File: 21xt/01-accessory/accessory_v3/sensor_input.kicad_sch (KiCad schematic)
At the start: 3 parts, among them J1 Conn_02x23_Counter_Clockwise, J2 Mezzanine Edge

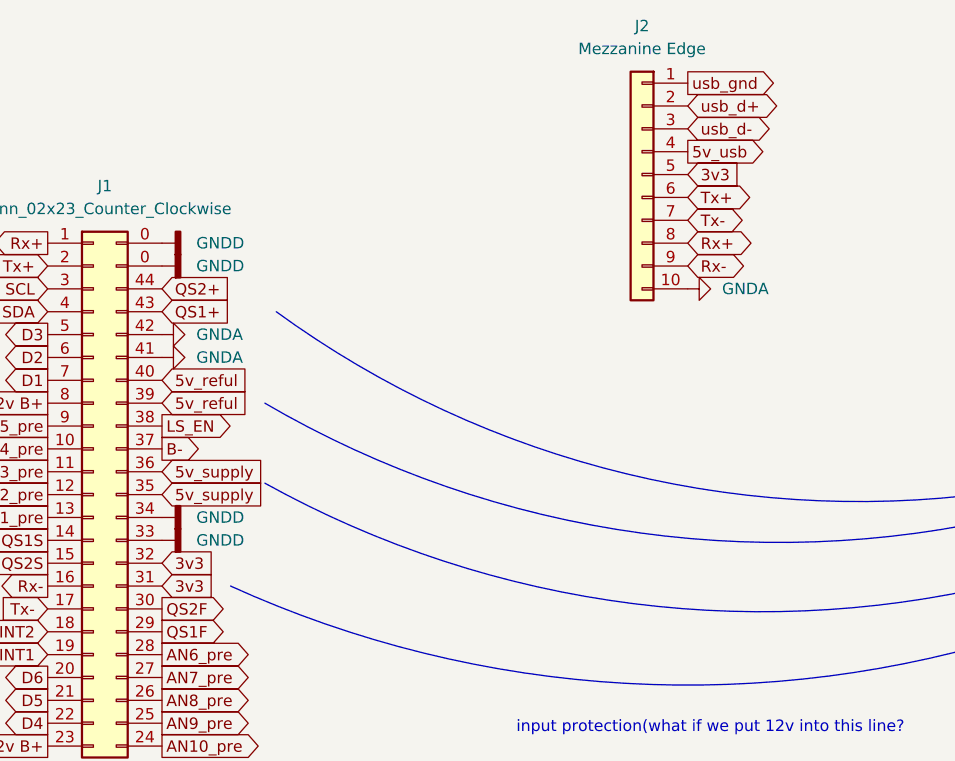
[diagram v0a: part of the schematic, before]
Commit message: Rerouted and connected 3v3 nets
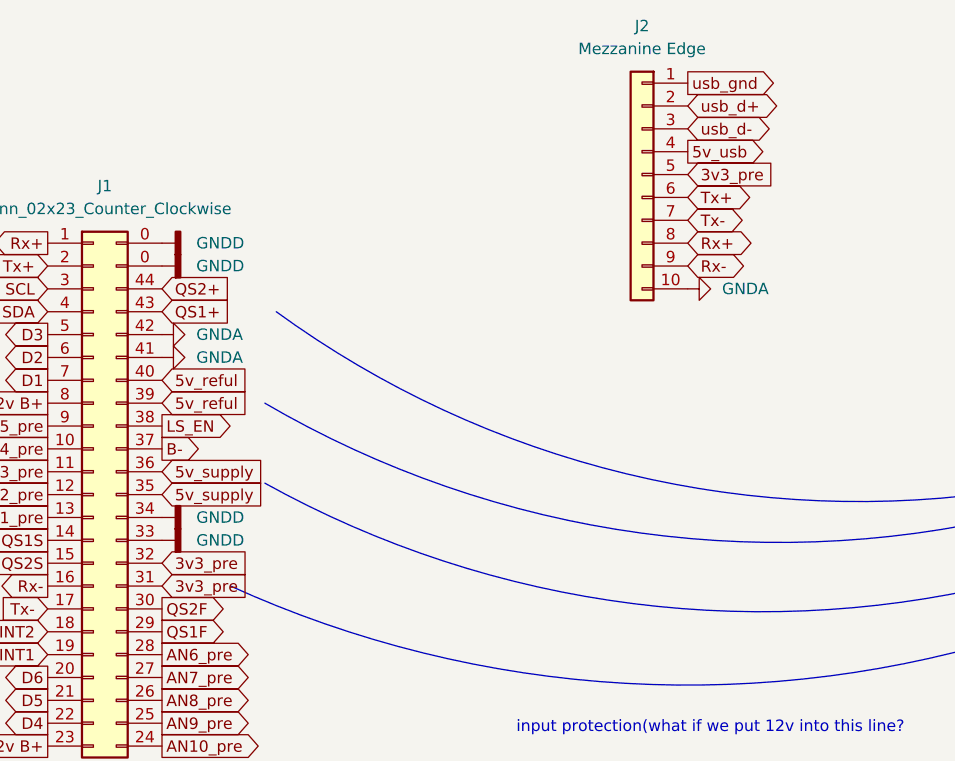
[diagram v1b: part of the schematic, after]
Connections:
- net 3v3 renamed 3v3_pre
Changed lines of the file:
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@@
 		)
 	)
-	(global_label "3v3"
-		(shape input)
-		(at 139.7 105.41 0)
-		(fields_autoplaced yes)
-		(effects
-			(font
-				(size 1.27 1.27)
-			)
-			(justify left)
-		)
-		(property "Intersheetrefs" "${INTERSHEET_REFS}"
-			(at 146.0718 105.41 0)
+	(global_label "3v3_pre"
+		(shape input)
+		(at 139.7 102.87 0)
+		(fields_autoplaced yes)
+		(effects
+			(font
+				(size 1.27 1.27)
+			)
+			(justify left)
+		)
+		(property "Intersheetrefs" "${INTERSHEET_REFS}"
+			(at 150.0632 102.87 0)
 			(effects
 				(font
@@
 				)
 				(justify right)
-				(hide yes)
-			)
-		)
-	)
-	(global_label "3v3"
-		(shape input)
-		(at 198.12 59.69 0)
-		(fields_autoplaced yes)
-		(effects
-			(font
-				(size 1.27 1.27)
-			)
-			(justify left)
-		)
-		(property "Intersheetrefs" "${INTERSHEET_REFS}"
-			(at 204.4918 59.69 0)
-			(effects
-				(font
-					(size 1.27 1.27)
-				)
-				(justify left)
 				(hide yes)
 			)
@@
 		)
 	)
+	(global_label "3v3_pre"
+		(shape input)
+		(at 139.7 105.41 0)
+		(fields_autoplaced yes)
+		(effects
+			(font
+				(size 1.27 1.27)
+			)
+			(justify left)
+		)
+		(property "Intersheetrefs" "${INTERSHEET_REFS}"
+			(at 150.0632 105.41 0)
+			(effects
+				(font
+					(size 1.27 1.27)
+				)
+				(justify left)
+				(hide yes)
+			)
+		)
+	)
 	(global_label "Tx-"
 		(shape input)
@@
 		)
 	)
-	(global_label "3v3"
-		(shape input)
-		(at 139.7 102.87 0)
-		(fields_autoplaced yes)
-		(effects
-			(font
-				(size 1.27 1.27)
-			)
-			(justify left)
-		)
-		(property "Intersheetrefs" "${INTERSHEET_REFS}"
-			(at 146.0718 102.87 0)
-			(effects
-				(font
-					(size 1.27 1.27)
-				)
-				(justify left)
-				(hide yes)
-			)
-		)
-	)
 	(global_label "usb_gnd"
 		(shape output)
@@
 			(effects
 				(font
+					(size 1.27 1.27)
+				)
+				(justify left)
+				(hide yes)
+			)
+		)
+	)
+	(global_label "3v3_pre"
+		(shape input)
+		(at 198.12 59.69 0)
+		(fields_autoplaced yes)
+		(effects
+			(font
+				(size 1.27 1.27)
+			)
+			(justify left)
+		)
+		(property "Intersheetrefs" "${INTERSHEET_REFS}"
+			(at 208.4832 59.69 0)
+			(effects
+				(font

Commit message: prod
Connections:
- net 3v3_pre renamed 3v3
- net 3v3: no longer J2.5 (Pin_5)
- new net 3v3_pre2: J2.5 (Pin_5)
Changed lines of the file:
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@@
+		)
+	)
+	(global_label "3v3"
+		(shape input)
+		(at 139.7 102.87 0)
+		(fields_autoplaced yes)
+		(effects
+			(font
+				(size 1.27 1.27)
+			)
+			(justify left)
+		)
+		(property "Intersheetrefs" "${INTERSHEET_REFS}"
+			(at 146.0718 102.87 0)
+			(effects
+				(font
+					(size 1.27 1.27)
+				)
+				(justify left)
+				(hide yes)
+			)
 		)
 	)
@@
 		)
 	)
-	(global_label "3v3_pre"
-		(shape input)
-		(at 139.7 102.87 0)
-		(fields_autoplaced yes)
-		(effects
-			(font
-				(size 1.27 1.27)
-			)
-			(justify left)
-		)
-		(property "Intersheetrefs" "${INTERSHEET_REFS}"
-			(at 150.0632 102.87 0)
-			(effects
-				(font
-					(size 1.27 1.27)
-				)
-				(justify left)
-				(hide yes)
-			)
-		)
-	)
 	(global_label "12v B+"
 		(shape output)
@@
 		)
 	)
+	(global_label "3v3_pre2"
+		(shape input)
+		(at 198.12 59.69 0)
+		(fields_autoplaced yes)
+		(effects
+			(font
+				(size 1.27 1.27)
+			)
+			(justify left)
+		)
+		(property "Intersheetrefs" "${INTERSHEET_REFS}"
+			(at 209.6927 59.69 0)
+			(effects
+				(font
+					(size 1.27 1.27)
+				)
+				(justify left)
+				(hide yes)
+			)
+		)
+	)
 	(global_label "GPIO{slash}INT2"
 		(shape bidirectional)
@@
 		)
 	)
+	(global_label "3v3"
+		(shape input)
+		(at 139.7 105.41 0)
+		(fields_autoplaced yes)
+		(effects
+			(font
+				(size 1.27 1.27)
+			)
+			(justify left)
+		)
+		(property "Intersheetrefs" "${INTERSHEET_REFS}"
+			(at 146.0718 105.41 0)
+			(effects
+				(font
+					(size 1.27 1.27)
+				)
+				(justify left)
+				(hide yes)
+			)
+		)
+	)
 	(global_label "AN7_pre"
 		(shape output)
@@
 		)
 	)
-	(global_label "3v3_pre"
-		(shape input)
-		(at 139.7 105.41 0)
-		(fields_autoplaced yes)
-		(effects
-			(font
-				(size 1.27 1.27)
-			)
-			(justify left)
-		)
-		(property "Intersheetrefs" "${INTERSHEET_REFS}"
-			(at 150.0632 105.41 0)
-			(effects
-				(font
-					(size 1.27 1.27)
-				)
-				(justify left)
-				(hide yes)
-			)
-		)
-	)
 	(global_label "Tx-"
 		(shape input)
@@
 			(effects
 				(font
-					(size 1.27 1.27)
-				)
-				(justify left)
-				(hide yes)
-			)
-		)
-	)
-	(global_label "3v3_pre"
-		(shape input)
-		(at 198.12 59.69 0)
-		(fields_autoplaced yes)
-		(effects
-			(font
-				(size 1.27 1.27)
-			)
-			(justify left)
-		)
-		(property "Intersheetrefs" "${INTERSHEET_REFS}"
-			(at 208.4832 59.69 0)
-			(effects
-				(font
